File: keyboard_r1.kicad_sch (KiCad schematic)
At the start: 1 part, among them J1 Conn_02x12_Top_Bottom

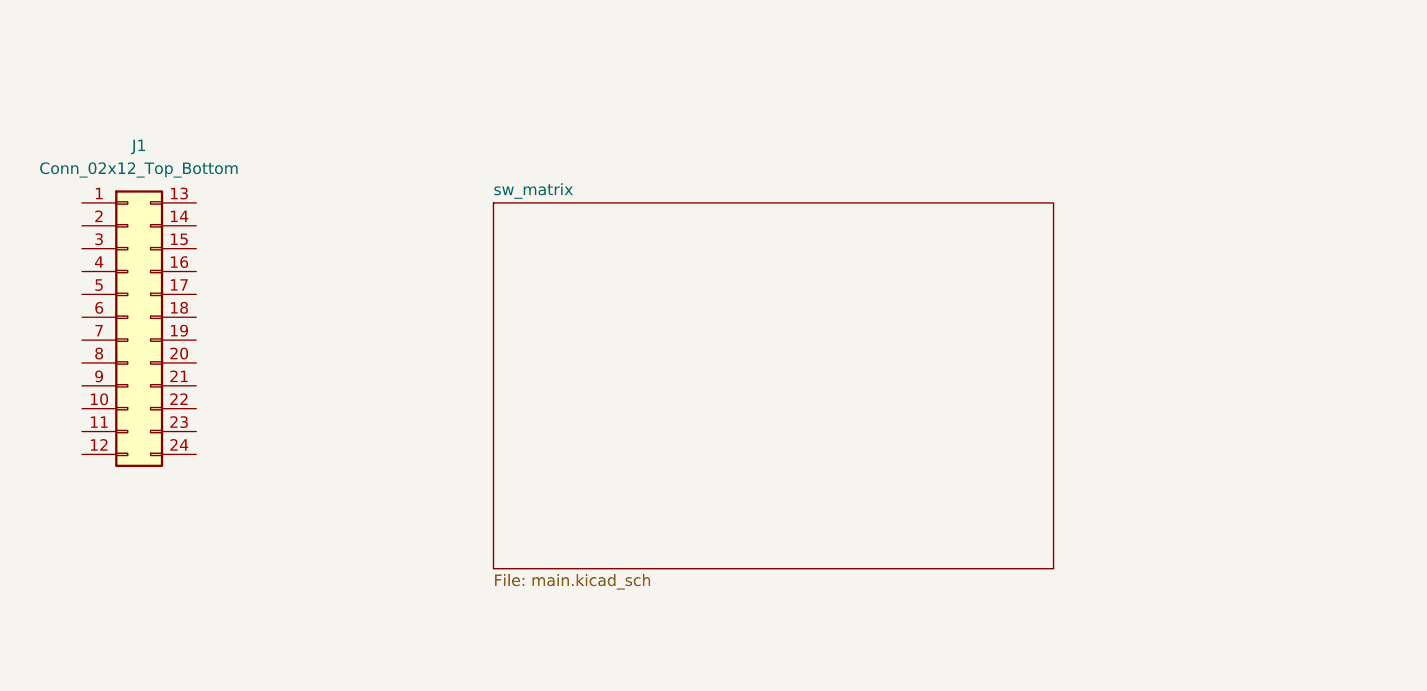
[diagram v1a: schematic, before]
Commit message: added Raspberry Pi Pico componenet
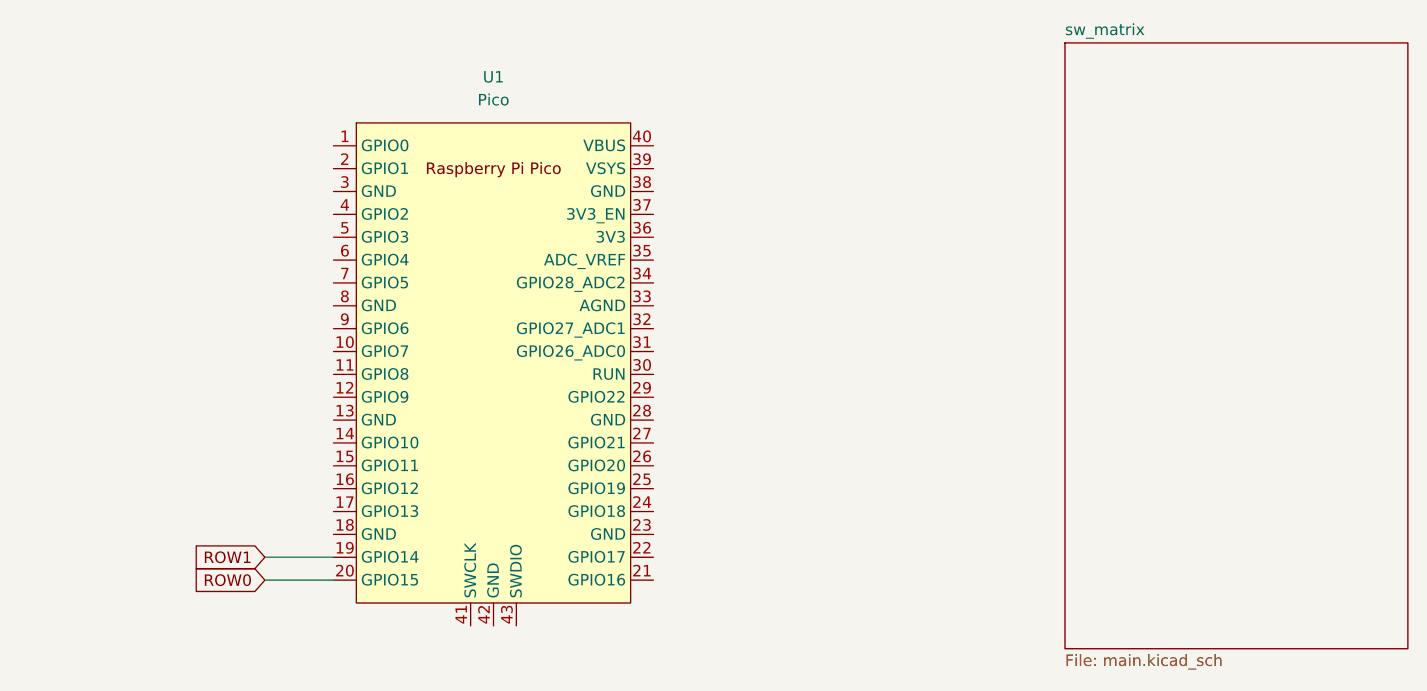
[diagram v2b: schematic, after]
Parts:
- removed J1: Conn_02x12_Top_Bottom, marbastlib-various:ProMicro, symbol Connector_Generic:Conn_02x12_Top_Bottom
- added U1: Pico, MCU_RaspberryPi_and_Boards:RPi_Pico_SMD_TH, symbol MCU_RaspberryPi_and_Boards:Pico
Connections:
- new net ROW0: U1.20 (GPIO15)
- new net ROW1: U1.19 (GPIO14)
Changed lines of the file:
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@@
 (kicad_sch (version 20211123) (generator eeschema)
   (paper "A5")
-  (symbol (lib_id "Connector_Generic:Conn_02x12_Top_Bottom") (at 52.07 55.88 0) (unit 1)
+  (wire (pts (xy 67.31 85.09) (xy 74.93 85.09))
+    (stroke (width 0) (type default) (color 0 0 0 0))
+  )
+  (wire (pts (xy 67.31 82.55) (xy 74.93 82.55))
+    (stroke (width 0) (type default) (color 0 0 0 0))
+  )
+  (global_label "ROW1" (shape input) (at 67.31 82.55 180) (fields_autoplaced)
+    (effects (font (size 1.27 1.27)) (justify right))
+    (property "Intersheet References" "${INTERSHEET_REFS}" (id 0) (at 59.6355 82.4706 0)
+      (effects (font (size 1.27 1.27)) (justify right) hide)
+    )
+  )
+  (global_label "ROW0" (shape input) (at 67.31 85.09 180) (fields_autoplaced)
+    (effects (font (size 1.27 1.27)) (justify right))
+    (property "Intersheet References" "${INTERSHEET_REFS}" (id 0) (at 59.6355 85.0106 0)
+      (effects (font (size 1.27 1.27)) (justify right) hide)
+    )
+  )
+  (symbol (lib_id "MCU_RaspberryPi_and_Boards:Pico") (at 92.71 60.96 0) (unit 1)
     (in_bom yes) (on_board yes) (fields_autoplaced)
-    (property "Reference" "J1" (id 0) (at 53.34 36.83 0))
-    (property "Value" "Conn_02x12_Top_Bottom" (id 1) (at 53.34 39.37 0))
-    (property "Footprint" "marbastlib-various:ProMicro" (id 2) (at 52.07 55.88 0)
+    (property "Reference" "U1" (id 0) (at 92.71 29.21 0))
+    (property "Value" "Pico" (id 1) (at 92.71 31.75 0))
+    (property "Footprint" "MCU_RaspberryPi_and_Boards:RPi_Pico_SMD_TH" (id 2) (at 92.71 60.96 90)
       (effects (font (size 1.27 1.27)) hide)
     )
-    (property "Datasheet" "~" (id 3) (at 52.07 55.88 0)
+    (property "Datasheet" "" (id 3) (at 92.71 60.96 0)
       (effects (font (size 1.27 1.27)) hide)
     )
@@
     (pin "23")
     (pin "24")
+    (pin "25")
+    (pin "26")
+    (pin "27")
+    (pin "28")
+    (pin "29")
     (pin "3")
+    (pin "30")
+    (pin "31")
+    (pin "32")
+    (pin "33")
+    (pin "34")
+    (pin "35")
+    (pin "36")
+    (pin "37")
+    (pin "38")
+    (pin "39")
     (pin "4")
+    (pin "40")
+    (pin "41")
+    (pin "42")
+    (pin "43")
     (pin "5")
     (pin "6")
@@
     (pin "9")
   )
-  (sheet (at 92.71 43.18) (size 62.23 40.64) (fields_autoplaced)
+  (sheet (at 156.21 25.4) (size 38.1 67.31) (fields_autoplaced)
     (stroke (width 0.1524) (type solid) (color 0 0 0 0))
     (fill (color 0 0 0 0.0000))
-    (property "Sheet name" "sw_matrix" (id 0) (at 92.71 42.4684 0)
+    (property "Sheet name" "sw_matrix" (id 0) (at 156.21 24.6884 0)
       (effects (font (size 1.27 1.27)) (justify left bottom))
     )
-    (property "Sheet file" "main.kicad_sch" (id 1) (at 92.71 84.4046 0)
+    (property "Sheet file" "main.kicad_sch" (id 1) (at 156.21 93.2946 0)
       (effects (font (size 1.27 1.27)) (justify left top))
     )
@@
       (reference "D76") (unit 1) (value "D_Small") (footprint "Diode_SMD:D_SOD-123")
     )
-    (path "/20a036ad-be67-4434-99dc-963059004e66"
-      (reference "J1") (unit 1) (value "Conn_02x12_Top_Bottom") (footprint "marbastlib-various:ProMicro")
-    )
     (path "/7942e31c-5f27-44a5-b5ea-0c8553a73ad2/2247ebc0-d72a-4f76-b81d-f0765c645894"
       (reference "S1") (unit 1) (value "MX_stab") (footprint "marbastlib-mx:STAB_MX_P_6u")
@@
       (reference "SW76") (unit 1) (value "MX_SW_solder") (footprint "marbastlib-mx:SW_MX_1u")
     )
-  )
+    (path "/c94d035e-fd5a-4808-8a73-4c9003636bfa"
+      (reference "U1") (unit 1) (value "Pico") (footprint "MCU_RaspberryPi_and_Boards:RPi_Pico_SMD_TH")
+    )
+  )

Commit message: added all global labels
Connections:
- net ROW0: no longer names the net of U1.20 (GPIO15)
- net ROW1: no longer names the net of U1.19 (GPIO14)
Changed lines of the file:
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@@
     (stroke (width 0) (type default) (color 0 0 0 0))
-  )
-  (global_label "ROW1" (shape input) (at 67.31 82.55 180) (fields_autoplaced)
-    (effects (font (size 1.27 1.27)) (justify right))
-    (property "Intersheet References" "${INTERSHEET_REFS}" (id 0) (at 59.6355 82.4706 0)
-      (effects (font (size 1.27 1.27)) (justify right) hide)
-    )
-  )
-  (global_label "ROW0" (shape input) (at 67.31 85.09 180) (fields_autoplaced)
-    (effects (font (size 1.27 1.27)) (justify right))
-    (property "Intersheet References" "${INTERSHEET_REFS}" (id 0) (at 59.6355 85.0106 0)
-      (effects (font (size 1.27 1.27)) (justify right) hide)
-    )
   )
   (symbol (lib_id "MCU_RaspberryPi_and_Boards:Pico") (at 92.71 60.96 0) (unit 1)
